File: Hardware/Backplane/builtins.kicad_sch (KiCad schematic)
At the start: 11 parts, among them J1001 Conn_01x06, J1002 Conn_01x06, J1003 Conn_01x06, J1004 Conn_01x06, SW1001 SW_Push, U1001 LTC6930CMS8-8.00#PBF

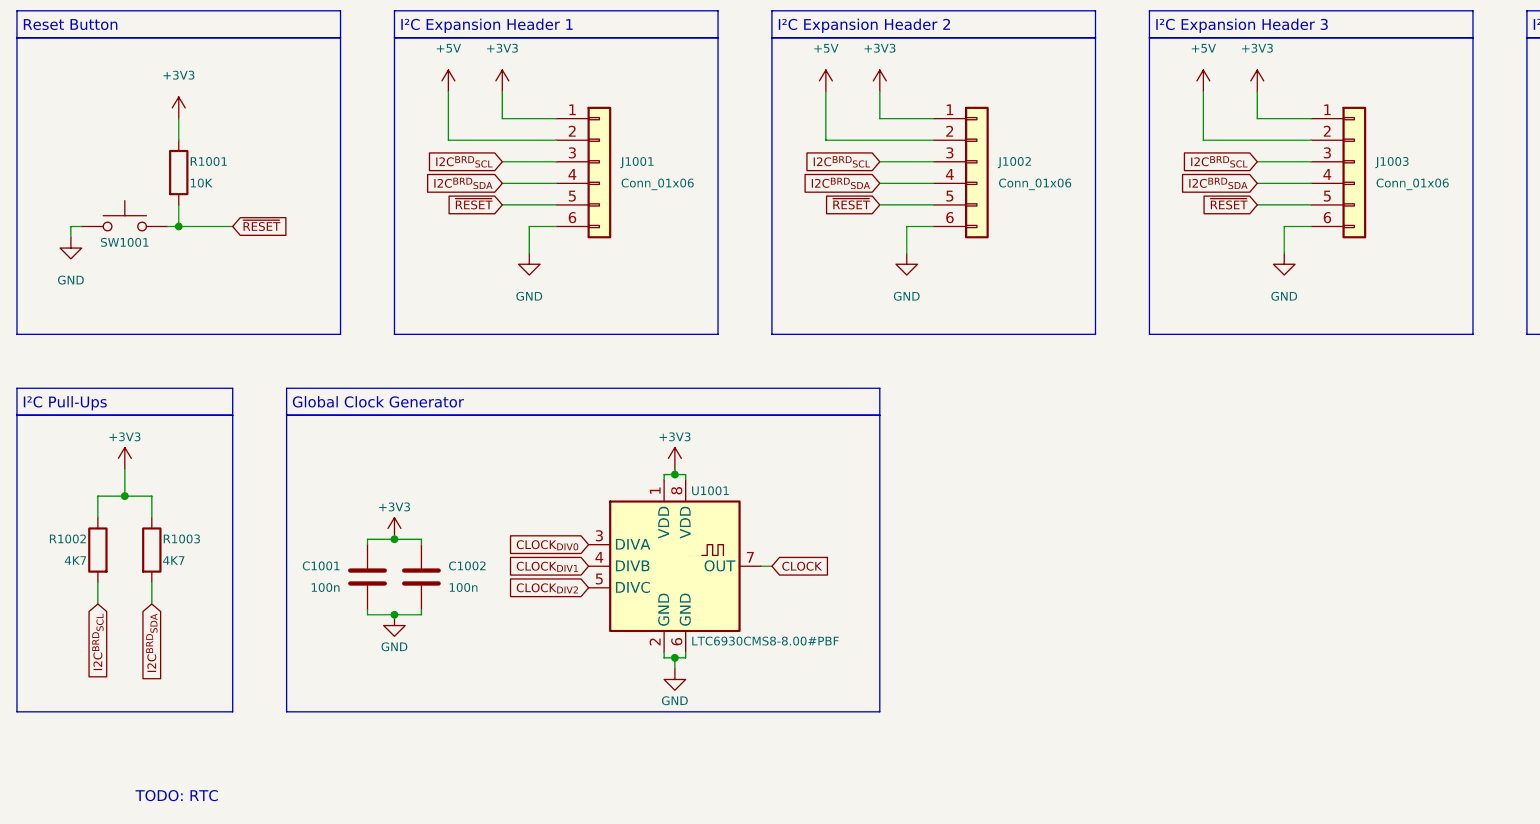
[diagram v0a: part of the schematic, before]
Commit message: Some work on the backplane schematics: Improves module locality
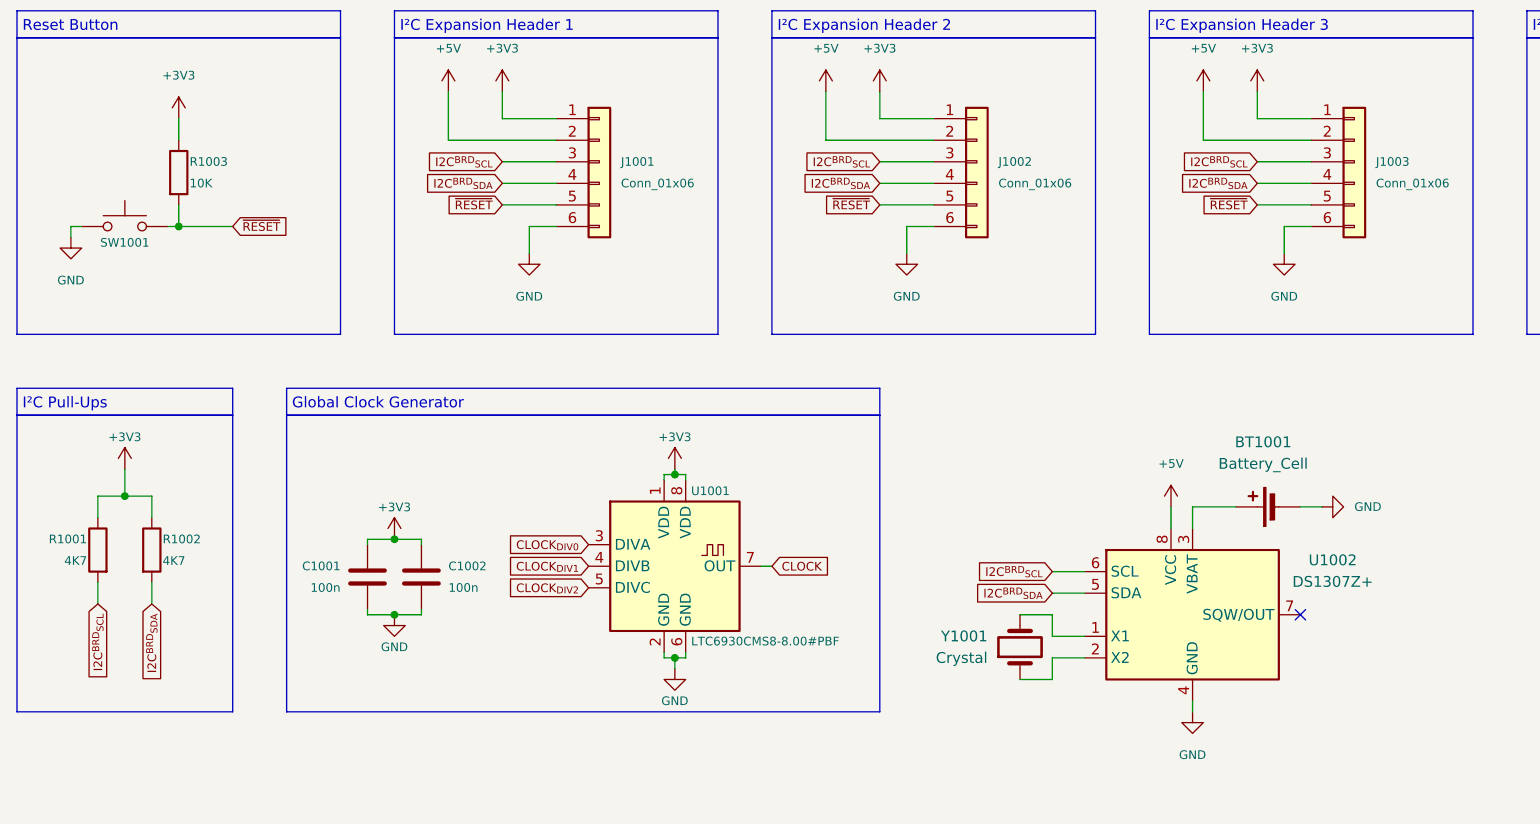
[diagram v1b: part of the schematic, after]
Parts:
- added BT1001: Battery_Cell, Battery:Battery_Panasonic_CR2032-HFN_Horizontal_CircularHoles, symbol Device:Battery_Cell
- added U1002: DS1307Z+, Package_SO:SOIC-8_3.9x4.9mm_P1.27mm, symbol Timer_RTC:DS1307Z+
- added Y1001: Crystal, symbol Device:Crystal
- renumbered R1002 to R1001, R1003 to R1002, R1001 to R1003
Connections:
- net +5V: now also U1002.8 (VCC)
- net GND: now also BT1001.2 (-), U1002.4 (GND)
- net I2C^{BRD}_{SCL}: now also U1002.6 (SCL)
- net I2C^{BRD}_{SDA}: now also U1002.5 (SDA)
- new net: U1002.2 (X2), Y1001.1
- new net: U1002.1 (X1), Y1001.2
- new net: BT1001.1 (+), U1002.3 (VBAT)
- no-connect marks 0 -> 1
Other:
- note removed: "TODO: RTC"

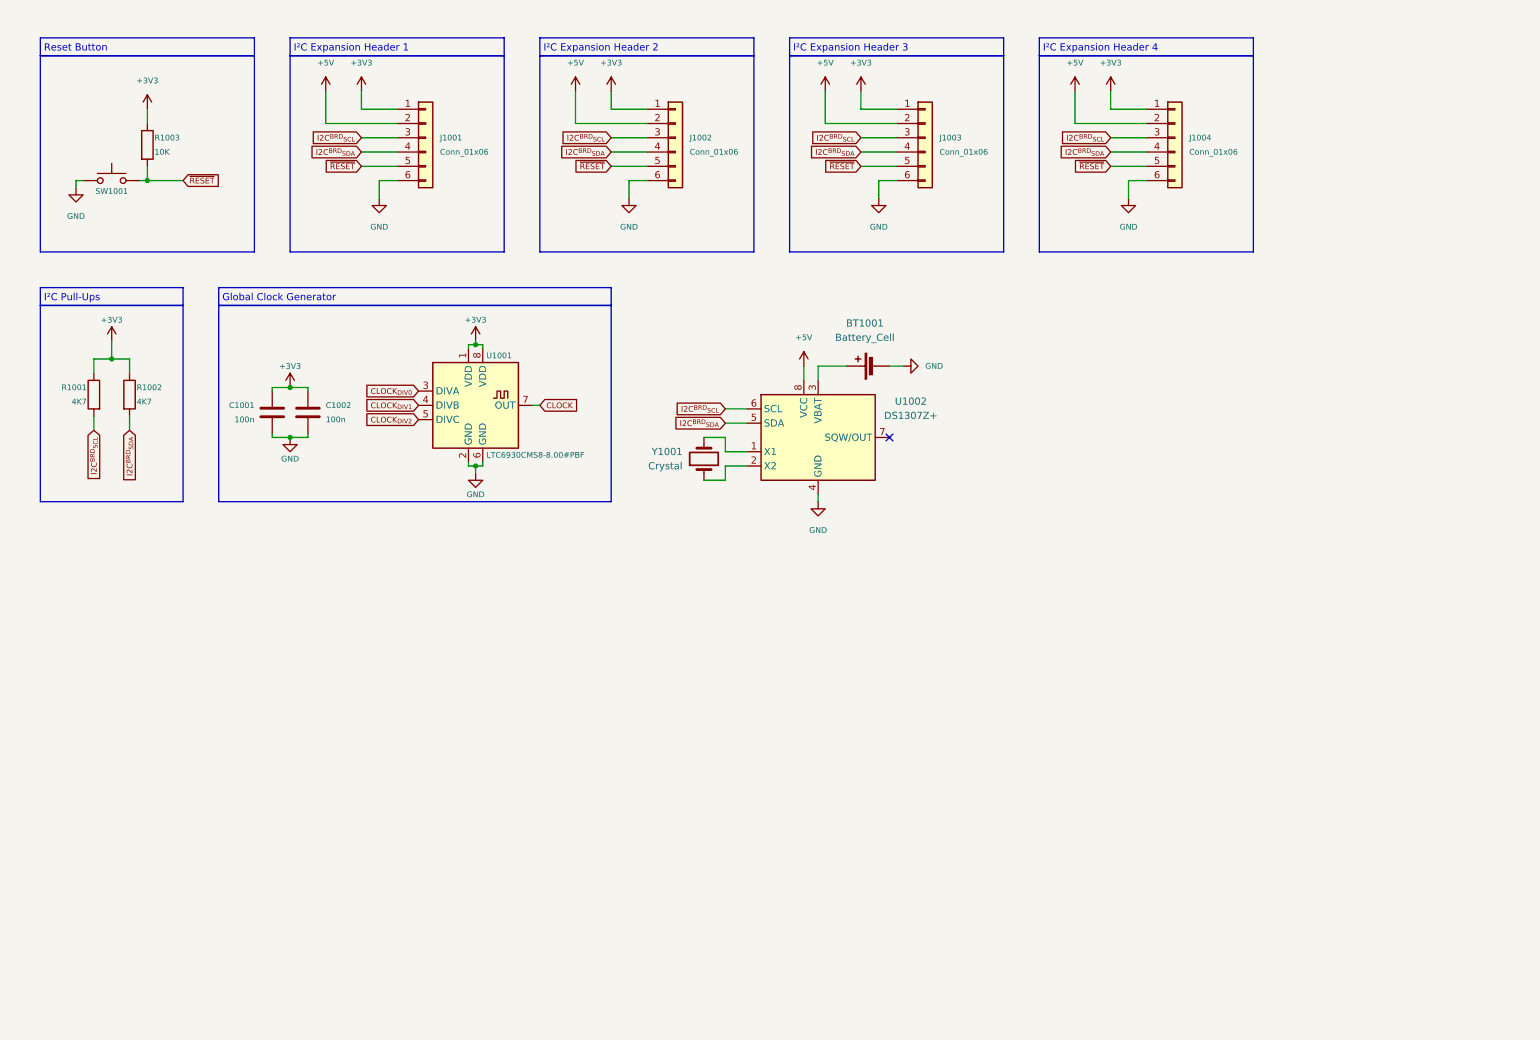
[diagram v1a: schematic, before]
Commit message: Starts to implement a tool to generate symbols for KiCAD from a generic description.
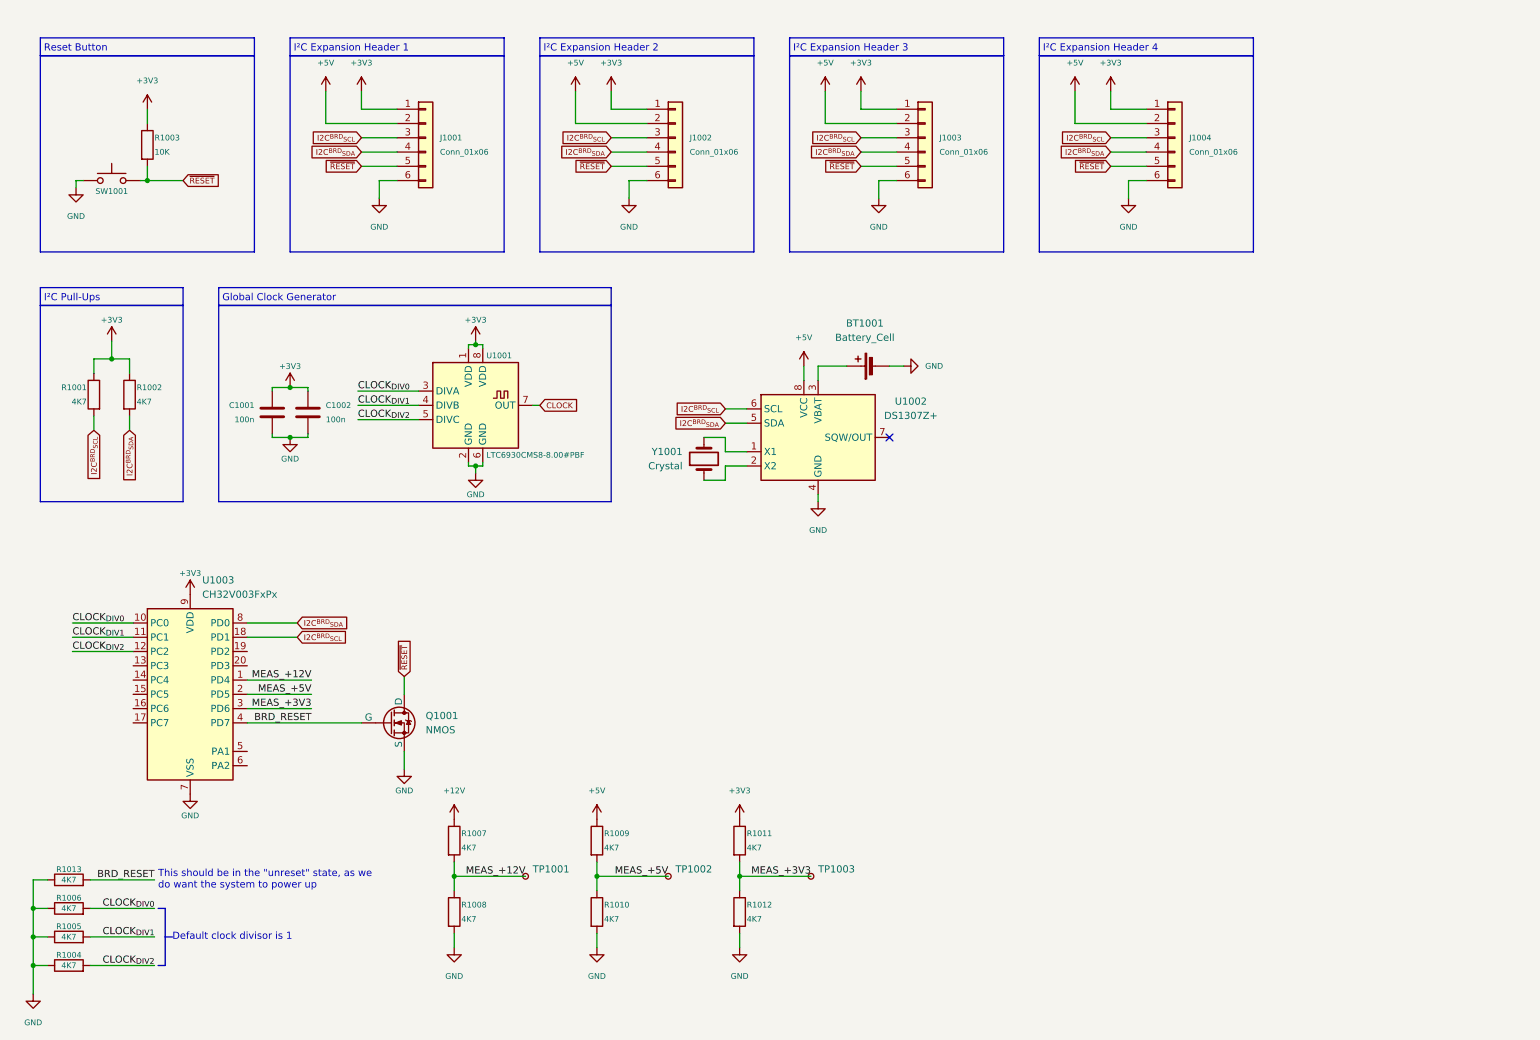
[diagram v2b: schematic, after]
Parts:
- added Q1001: NMOS, Package_TO_SOT_SMD:SOT-23, symbol Simulation_SPICE:NMOS
- added R1004, R1005, R1006, R1007, R1008, R1009, R1010, R1011, R1012, R1013: 4K7, Resistor_SMD:R_0603_1608Metric, symbol Device:R
- added TP1001, TP1002, TP1003: TestPoint_Small, TestPoint:TestPoint_Pad_D1.0mm, symbol Connector:TestPoint_Small
- added U1003: CH32V003FxPx, Package_SO:TSSOP-20_4.4x6.5mm_P0.65mm, symbol MCU_WCH_CH32V0:CH32V003FxPx
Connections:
- net +3V3: now also R1011.1, U1003.9 (VDD)
- net +5V: now also R1009.1
- net CLOCK_{DIV0}: now also R1006.2, U1003.10 (PC0)
- net CLOCK_{DIV1}: now also R1005.2, U1003.11 (PC1)
- net CLOCK_{DIV2}: now also R1004.2, U1003.12 (PC2)
- net GND: now also Q1001.3 (S), R1004.1, R1005.1, R1006.1, R1008.2, R1010.2, R1012.2, R1013.1, U1003.7 (VSS)
- net I2C^{BRD}_{SCL}: now also U1003.18 (PD1)
- net I2C^{BRD}_{SDA}: now also U1003.8 (PD0)
- net ~{RESET}: now also Q1001.1 (D)
- new net +12V: R1007.1
- new net BRD_RESET: Q1001.2 (G), R1013.2, U1003.4 (PD7)
- new net MEAS_+12V: R1007.2, R1008.1, TP1001.1, U1003.1 (PD4)
- new net MEAS_+3V3: R1011.2, R1012.1, TP1003.1, U1003.3 (PD6)
- new net MEAS_+5V: R1009.2, R1010.1, TP1002.1, U1003.2 (PD5)
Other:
- note added: "Default clock divisor is 1"
- note added: "This should be in the "unreset" state, as we do want the system to power up"

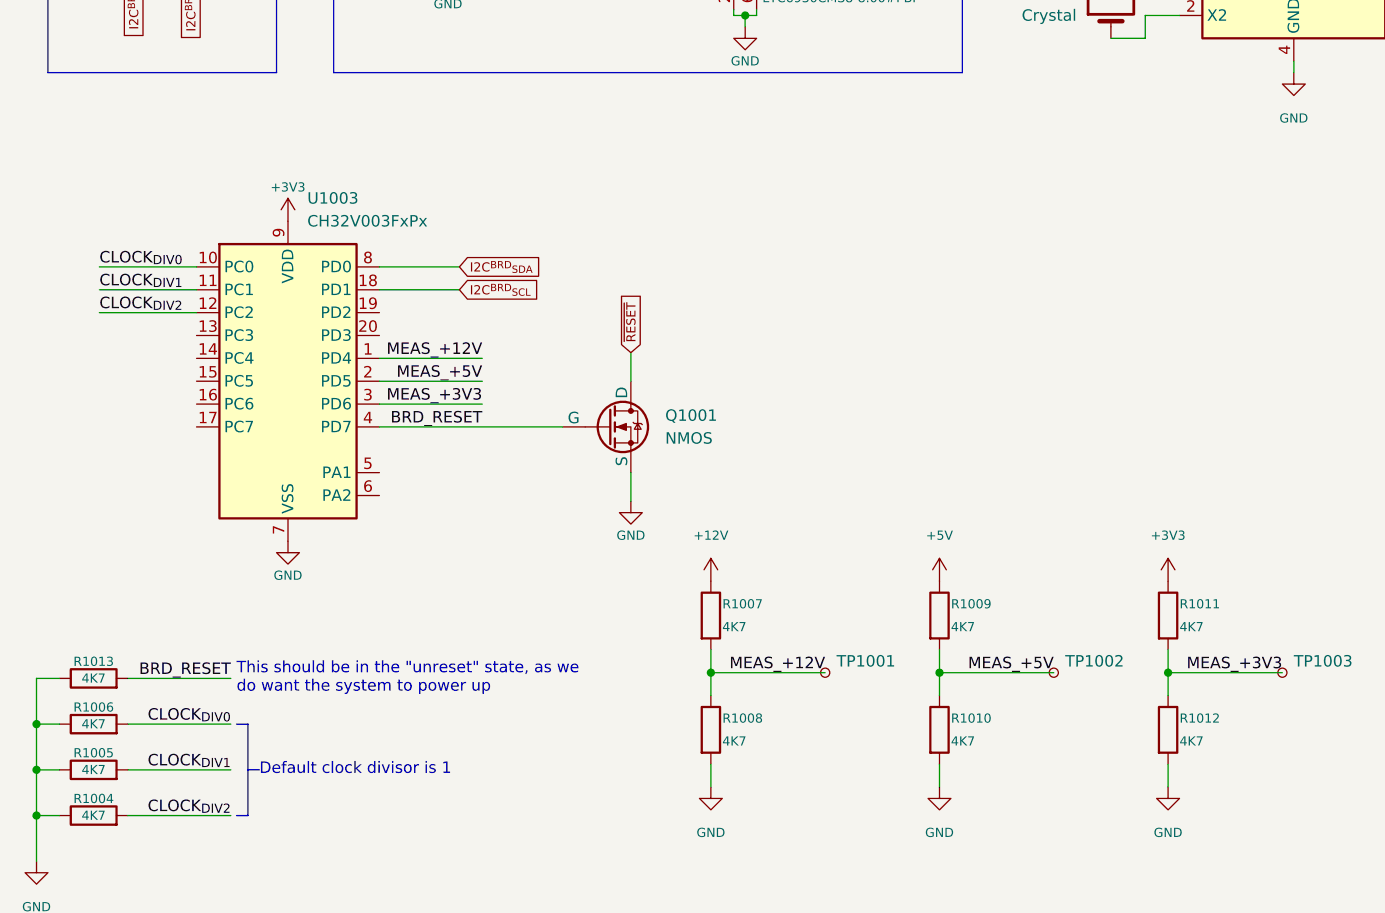
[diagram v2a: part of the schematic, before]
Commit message: Cleans up the backplane schematic and improves on features a lot.
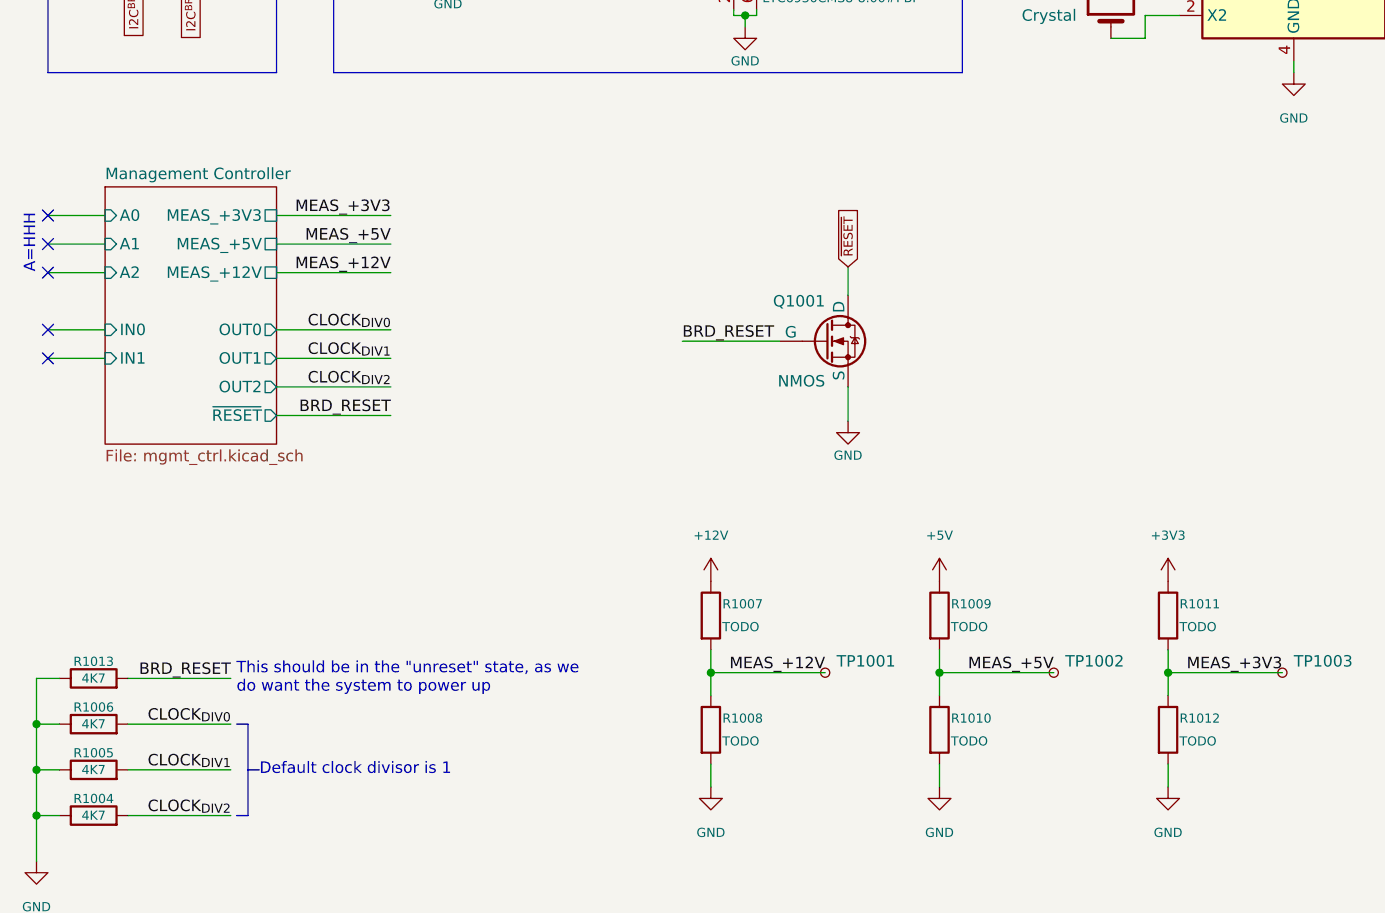
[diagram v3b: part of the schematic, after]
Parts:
- removed U1003: CH32V003FxPx, Package_SO:TSSOP-20_4.4x6.5mm_P0.65mm, symbol MCU_WCH_CH32V0:CH32V003FxPx
- R1007, R1008, R1009, R1010, R1011, R1012: value 4K7 -> TODO
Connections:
- no-connect marks 1 -> 6
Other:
- added sheet Management Controller (mgmt_ctrl.kicad_sch)
- note added: "A=HHH"
- moved on the sheet: Q1001
